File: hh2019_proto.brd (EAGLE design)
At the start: 80.8 x 165.7 mm, 123 parts, among them IC1 CP210X_USB_UART, IC2 AP2114H, IC4 TP4056, J1 PJ-313D, Q1 MMBT2222A, Q3 MMBT2222A, Q4 MMBT2222A, Q5 SI1304 BDL, U1 MPR121QR2, U2 ESP32-WROVER-I, U3 PCM5102A, X4 JST-PH3

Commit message: Added moar cybar
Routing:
- net CE: track 16.4 -> 29.7 mm, vias 0 -> 2
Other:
- board text added: "'s CYBER"
- board text added: "RX"
- board text added: "TX"
- board text added: "rev 1.0.0"
- board text removed: "Hackerhotel 2019 Event Badge PROTO 2"
- board text removed: "rev 0.0.2"
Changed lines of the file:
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@@
 <layer number="28" name="bValues" color="7" fill="1" visible="no" active="yes"/>
 <layer number="29" name="tStop" color="7" fill="3" visible="yes" active="yes"/>
-<layer number="30" name="bStop" color="7" fill="6" visible="no" active="yes"/>
+<layer number="30" name="bStop" color="7" fill="6" visible="yes" active="yes"/>
 <layer number="31" name="tCream" color="7" fill="4" visible="no" active="yes"/>
 <layer number="32" name="bCream" color="7" fill="5" visible="no" active="yes"/>
@@
 <text x="48.302" y="127.918" size="1.778" layer="26" rot="MR90">Power</text>
 <text x="77.702" y="159.118" size="1.4224" layer="26" rot="MR90">F1</text>
-<text x="56.322" y="48.518" size="2.1844" layer="26" font="vector" rot="MR0" align="top-center">Hackerhotel 2019
-Event Badge
-PROTO 2</text>
-<text x="83.203" y="26.609" size="1.27" layer="26" rot="MR0">rev 0.0.2</text>
-<text x="29.652" y="21.848" size="1.27" layer="26" rot="MR0" align="bottom-right">Designed &amp; produced by
+<text x="25.203" y="10.609" size="1.27" layer="26" rot="MR0">rev 1.0.0</text>
+<text x="18.152" y="13.948" size="1.27" layer="26" rot="MR0" align="bottom-right">Designed &amp; produced by
 badge.team</text>
 <polygon width="0.2" layer="42">
@@
 <text x="36" y="73" size="0.6096" layer="26" font="vector" rot="MR270">SDA</text>
 <text x="32" y="73" size="0.6096" layer="26" font="vector" rot="MR270">SCL</text>
+<text x="39.4" y="138.3" size="0.4064" layer="25" rot="R90">RX</text>
+<text x="39.4" y="135.8" size="0.4064" layer="25" rot="R90">TX</text>
+<text x="28" y="167" size="15" layer="30" font="vector" ratio="16" rot="MR270">'s CYBER</text>
+<polygon width="0.2" layer="26">
+<vertex x="30" y="57"/>
+<vertex x="14" y="57"/>
+<vertex x="14" y="18"/>
+<vertex x="30" y="18"/>
+</polygon>
 </plain>
 <attributes>
@@
 <wire x1="57.07955625" y1="65.4581" x2="56.773278125" y2="65.764378125" width="0.2" layer="16"/>
 <wire x1="56.773278125" y1="65.764378125" x2="56.375621875" y2="65.764378125" width="0.2" layer="16"/>
-<wire x1="69.062" y1="155.968" x2="69.1596" y2="156.0656" width="0.2" layer="16"/>
-<wire x1="69.1596" y1="156.0656" x2="69.66655" y2="156.0656" width="0.2" layer="16"/>
 <wire x1="70.06895" y1="156.468" x2="71.562" y2="156.468" width="0.2" layer="16"/>
-<wire x1="69.66655" y1="156.0656" x2="70.06895" y2="156.468" width="0.2" layer="16"/>
 <via x="71.562" y="156.468" extent="1-16" drill="0.4"/>
 <wire x1="42.082" y1="86.348" x2="42.352" y2="86.618" width="0.2" layer="16"/>
@@
 <via x="63.942" y="90.428" extent="1-16" drill="0.4"/>
 <wire x1="71.192" y1="165.008" x2="71.192" y2="166.858" width="0.2" layer="16"/>
-<wire x1="68.45745" y1="155.8704" x2="68.3096" y2="155.72255" width="0.2" layer="16"/>
 <wire x1="68.3096" y1="154.71345" x2="68.45745" y2="154.5656" width="0.2" layer="16"/>
 <wire x1="68.45745" y1="154.5656" x2="69.2594" y2="154.5656" width="0.2" layer="16"/>
 <wire x1="69.2594" y1="154.5656" x2="69.4595" y2="154.3655" width="0.2" layer="16"/>
 <wire x1="68.3096" y1="155.72255" x2="68.3096" y2="154.71345" width="0.2" layer="16"/>
-<wire x1="69.062" y1="155.968" x2="68.9644" y2="155.8704" width="0.2" layer="16"/>
-<wire x1="68.9644" y1="155.8704" x2="68.45745" y2="155.8704" width="0.2" layer="16"/>
 <wire x1="74.742" y1="148.768" x2="75.372" y2="149.398" width="0.2" layer="16"/>
 <wire x1="75.372" y1="149.398" x2="75.372" y2="150.118" width="0.2" layer="16"/>
@@
 <wire x1="76" y1="84" x2="76" y2="85.286" width="0.2" layer="16"/>
 <contactref element="SHITTY-ADDON" pad="1"/>
+<wire x1="69.062" y1="155.968" x2="69.56895" y2="155.968" width="0.2" layer="16"/>
+<wire x1="69.56895" y1="155.968" x2="70.06895" y2="156.468" width="0.2" layer="16"/>
+<wire x1="69.062" y1="155.968" x2="68.55505" y2="155.968" width="0.2" layer="16"/>
+<wire x1="68.55505" y1="155.968" x2="68.3096" y2="155.72255" width="0.2" layer="16"/>
 <wire x1="71.192" y1="166.858" x2="70.742" y2="167.308" width="0" layer="19" extent="16-16"/>
 <wire x1="57.902528125" y1="64.561025" x2="57.902525" y2="64.561025" width="0" layer="19" extent="16-16"/>
@@
 <wire x1="55.372" y1="105.668" x2="55.372" y2="109.378" width="0.2" layer="16"/>
 <wire x1="55.372" y1="109.378" x2="55.472" y2="109.478" width="0.2" layer="16"/>
-<wire x1="45.667" y1="99.953" x2="51.737" y2="96.143" width="0" layer="19" extent="16-16"/>
+<wire x1="45.667" y1="99.953" x2="46.6698" y2="99.953" width="0.2" layer="16"/>
+<wire x1="46.6698" y1="99.953" x2="46.7" y2="99.9832" width="0.2" layer="16"/>
+<via x="46.7" y="99.9832" extent="1-16" drill="0.4"/>
+<wire x1="46.7" y1="99.9832" x2="48.0168" y2="101.3" width="0.2" layer="1"/>
+<wire x1="51" y1="101" x2="51" y2="95.5" width="0.2" layer="1"/>
+<wire x1="51" y1="95.5" x2="51.2" y2="95.3" width="0.2" layer="1"/>
+<wire x1="51.2" y1="95.3" x2="51.6" y2="95.3" width="0.2" layer="1"/>
+<wire x1="51.6" y1="95.3" x2="51.7" y2="95.2" width="0.2" layer="1"/>
+<via x="51.7" y="95.2" extent="1-16" drill="0.4"/>
+<wire x1="51.7" y1="95.2" x2="51.737" y2="95.237" width="0.2" layer="16"/>
+<wire x1="51.737" y1="95.237" x2="51.737" y2="96.143" width="0.2" layer="16"/>
+<wire x1="50.7" y1="101.3" x2="51" y2="101" width="0.2" layer="1"/>
+<wire x1="48.0168" y1="101.3" x2="50.7" y2="101.3" width="0.2" layer="1"/>
 </signal>
 <signal name="N$20">

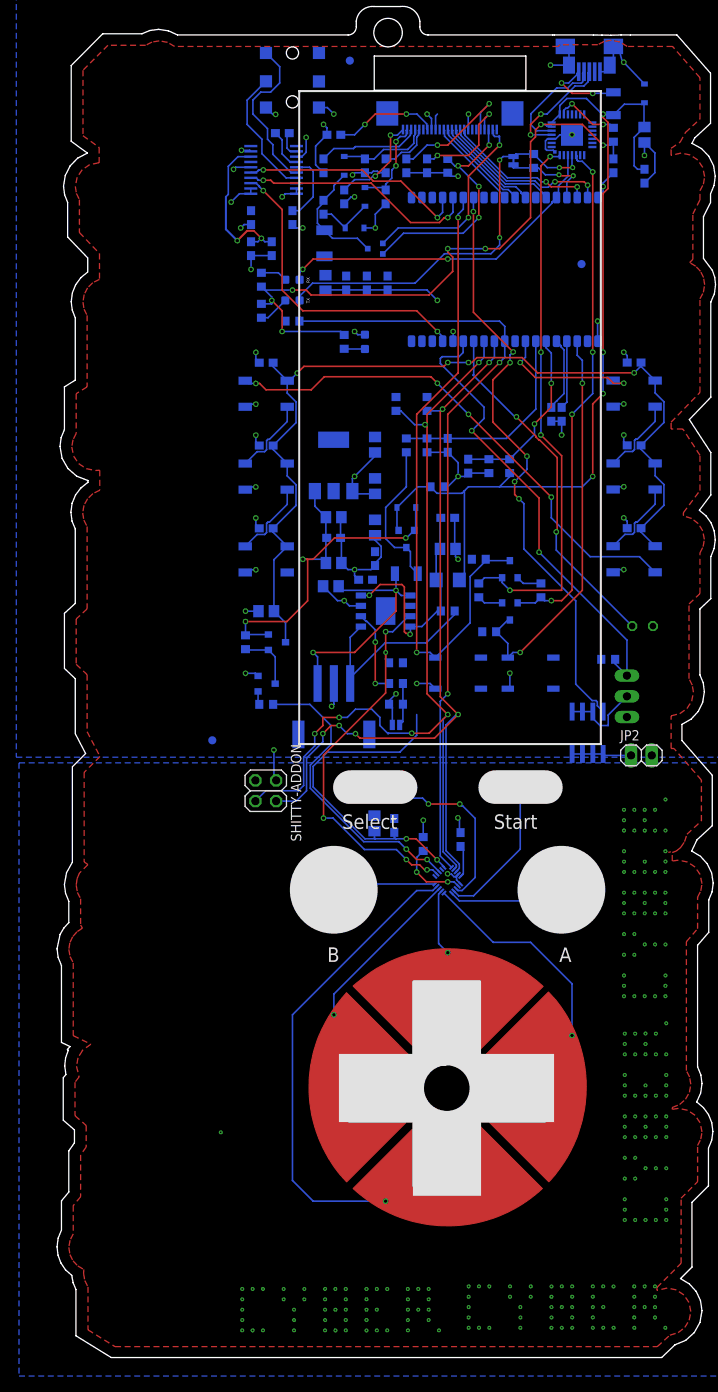
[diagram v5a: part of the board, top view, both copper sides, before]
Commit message: Added Renze's superfluous Grove connector
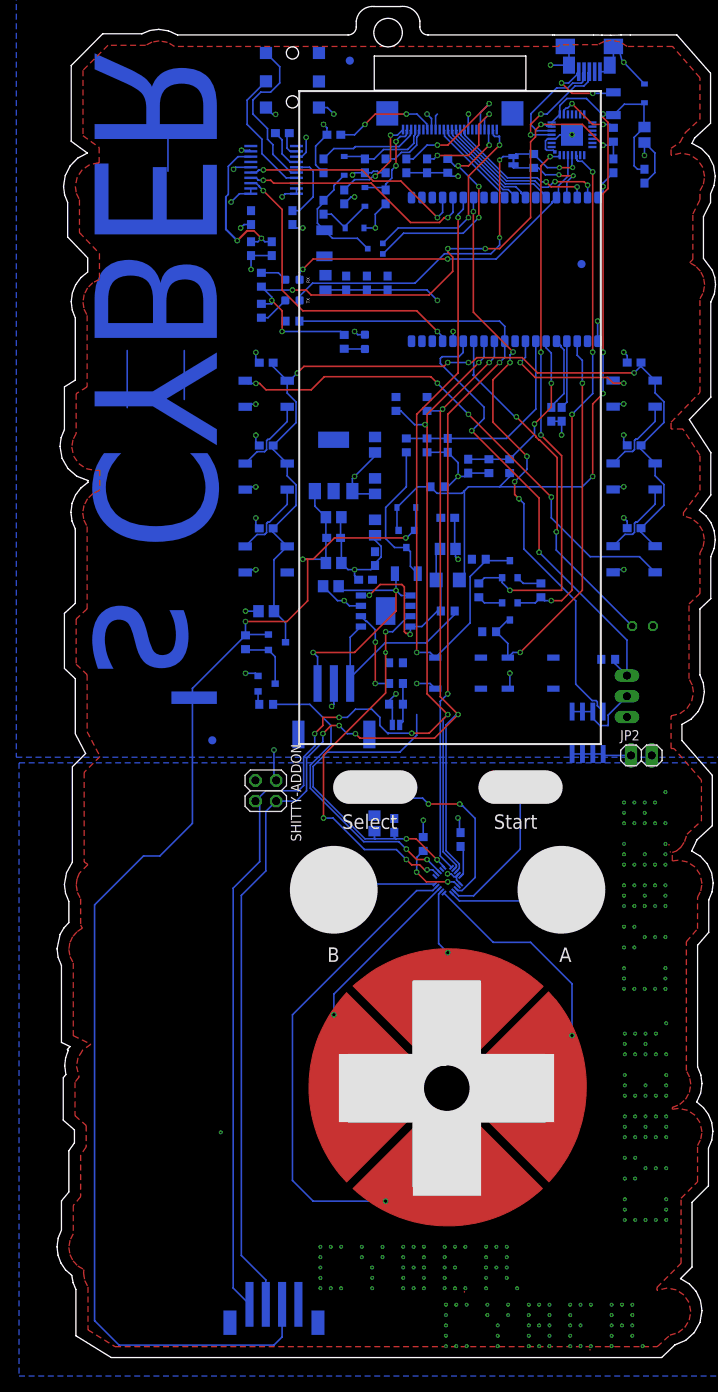
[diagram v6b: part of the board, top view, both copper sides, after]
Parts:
- added P1: B4B-PH-SM4-TB, B4B-PH-SM4-TB:JST_B4B-PH-SM4-TB
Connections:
- net GND: now also P1.4
- net I2C_SCL: now also P1.1
- net I2C_SDA: now also P1.2
- net VCC: now also P1.3
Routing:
- net VCC: track 49.4 -> 171.0 mm
- net I2C_SDA: track 103.3 -> 168.0 mm
- net I2C_SCL: track 108.8 -> 173.0 mm
- net 3V3: track 47.2 -> 64.2 mm
- net N$90: track 0.00 -> 0.07 mm, vias 1 -> 0
- net N$193: track 0.00 -> 0.07 mm, vias 1 -> 0

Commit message: Finished design, exported BOM and centroid files, and created gerbers
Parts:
- removed JP2: (no value), pinhead:1X02
- removed Q2: (no value), transistor-power:SO-08
- added BUZZ1: (no value), pinhead:1X02
- added Q6: SI1304 BDL, SparkFun-DiscreteSemi:SOT323
- renumbered LED1 to IR_LED
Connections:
- net 3V3: now also BUZZ1.2; no longer JP2.2
- net BUZZER: now also Q6.1; no longer Q2.4
- net BUZZ_OUT: now also BUZZ1.1, Q6.3; no longer JP2.1, Q2.5, Q2.6, Q2.7, Q2.8
- net GND: now also Q6.2; no longer Q2.1, Q2.2, Q2.3
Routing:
- net GND: track 205.1 -> 200.3 mm
- net BUZZ_OUT: track 7.30 -> 10.0 mm
- net BUZZER: track 73.3 -> 71.7 mm
- net VCC: track 171.0 -> 171.5 mm
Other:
- board text added: "'s"
- board text added: "0b49 40e2 7274 b7b8 80e4 3cfe 66a9 518c"
- board text added: "AES all the things"
- board text added: "CYBER"
- board text added: "PCB House, put batch ID here: >> <<"
- board text added: "USB1"
- board text removed: "'s CYBER"
